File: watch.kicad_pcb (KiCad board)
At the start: 2 copper layers, 27.5 x 28.5 mm, 66 parts, among them M1 3V3 35mA, Q1 IRLML6302, Q2 IRLML0060TRPbF, SW1 B3U-3000P, SW2 B3U-3000P, SW3 B3U-3000P, X2 209E-BE01, X3 OLED I2C

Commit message: Add flash connector for stm32f3discovery stlink
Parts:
- added X1: SWD, Pin_Headers:Pin_Header_Straight_1x06, F.Cu at (61.5, 34.8)
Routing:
- net /~RES: track 21.6 -> 38.2 mm, vias 2 -> 4
- net /SWDIO: track 9.88 -> 21.3 mm, vias 0 -> 1
- net /SWCLK: track 9.23 -> 18.4 mm, vias 0 -> 1
- net GND: track 259.0 -> 263.8 mm, vias 33 -> 37
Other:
- board size 27.5 x 28.5 mm -> 33.2 x 28.5 mm

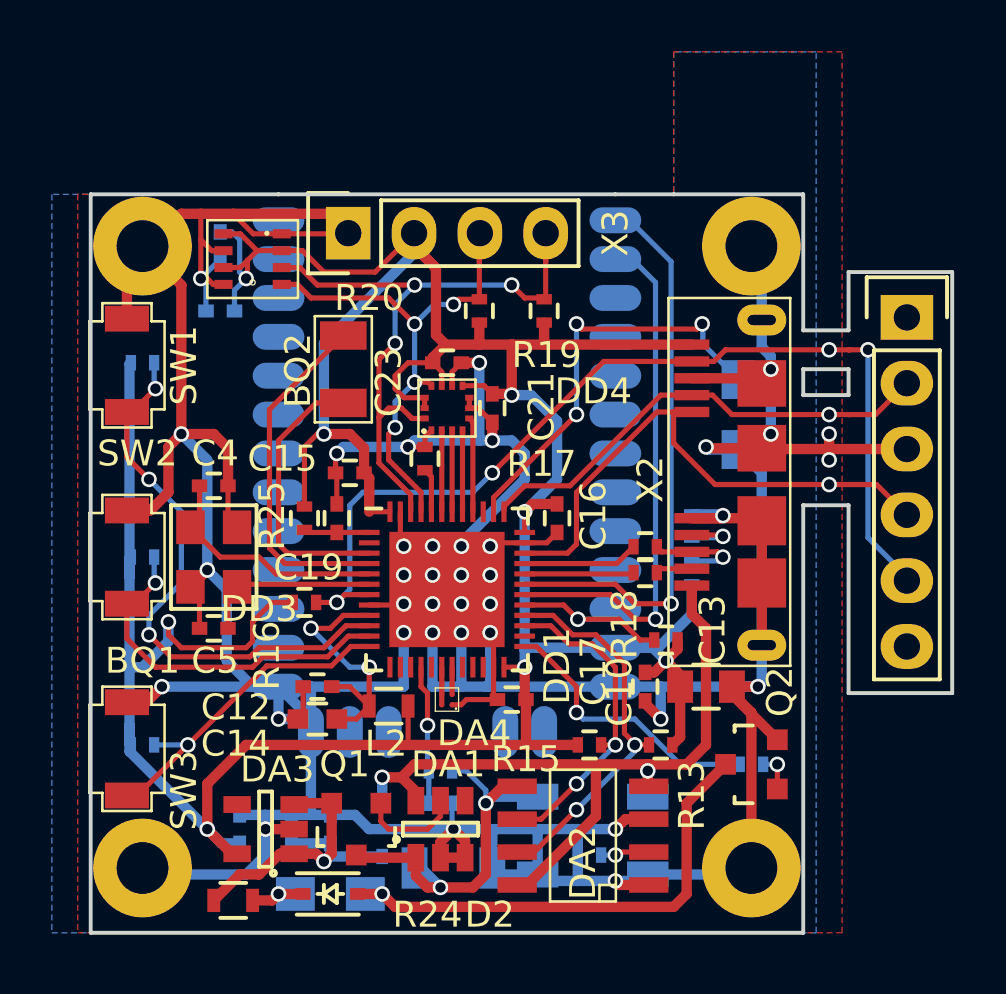
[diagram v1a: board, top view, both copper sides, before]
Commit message: Fixed MCU footprint
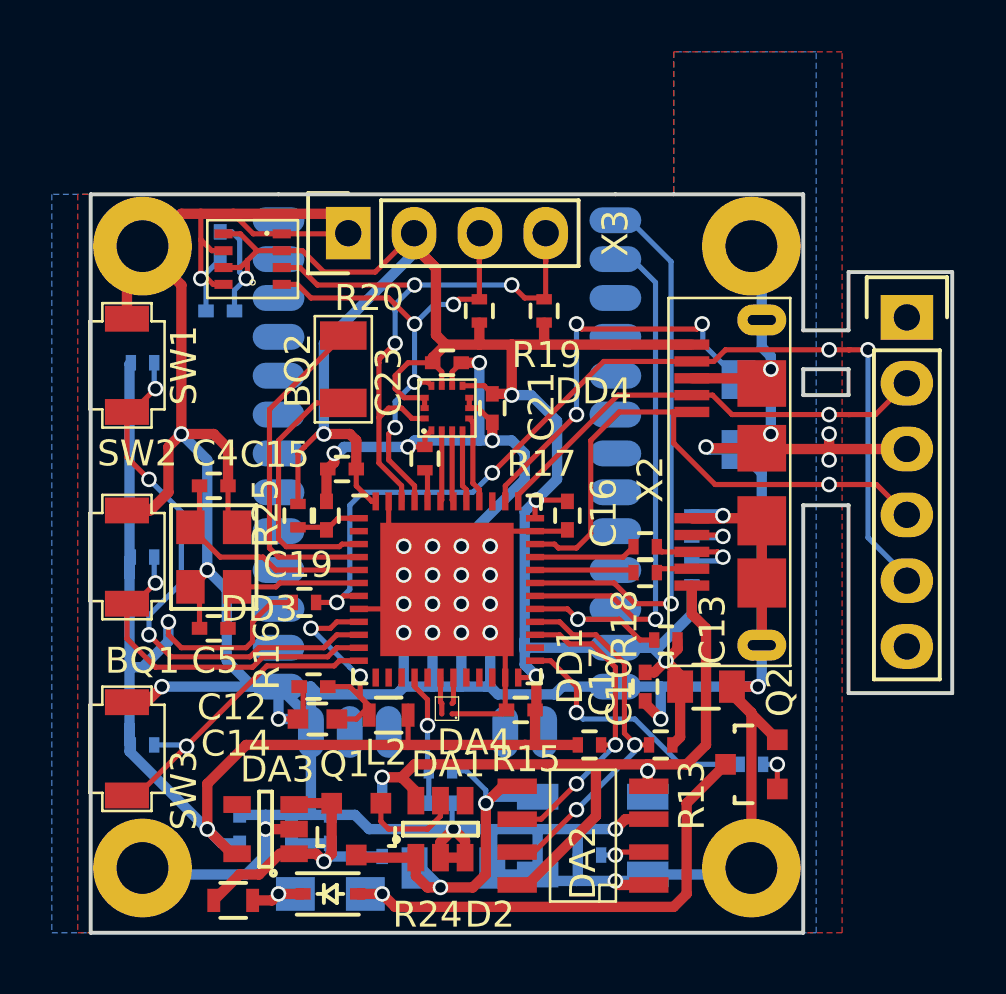
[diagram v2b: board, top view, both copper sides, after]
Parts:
- DD1: footprint Housings_DFN_QFN:UQFN-48-1EP_6x6mm_Pitch0.4mm -> Housings_DFN_QFN:QFN-48-1EP_7x7mm_Pitch0.5mm
- moved C17 0.53 mm to (46.6, 49.9)
- moved C16 0.41 mm to (48.4, 42.4)
- moved C19 0.41 mm to (39.1, 42.4)
- moved DA4 0.35 mm to (43.8, 49.9)
- moved L2 0.35 mm to (41.5, 50.1)
- moved C15 0.34 mm to (39.7, 40.6)
- moved R25 0.27 mm to (38.0, 42.4)
- moved C12 0.15 mm to (38.6, 49.0)
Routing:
- net GND: track 263.8 -> 267.0 mm
- net VAA: track 10.0 -> 9.33 mm
- net /SWCLK: track 18.4 -> 17.7 mm
- net /VIBRO: track 10.8 -> 10.1 mm
- net /BTN1: track 14.1 -> 13.5 mm
- net /BEEP: track 16.5 -> 15.9 mm
- net Net-(BQ2-Pad2): track 10.7 -> 10.2 mm
- net /~STDBY: track 12.7 -> 12.1 mm
- net /I2C_SDA: track 26.3 -> 25.7 mm
- net /BTN0: track 21.8 -> 21.3 mm
- net /SWDIO: track 21.3 -> 21.8 mm
- net Net-(BQ2-Pad1): track 13.5 -> 13.0 mm
- net /~CHRG: track 14.9 -> 14.4 mm
- net /USB_DP: track 4.47 -> 3.97 mm
- net /I2C_SCL: track 20.9 -> 20.4 mm
